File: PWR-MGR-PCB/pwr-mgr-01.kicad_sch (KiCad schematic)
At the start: 25 parts, among them J2 Battery_1x2, J3 USB_C_Receptacle_USB2.0_14P, U1 BQ24075, U5 USBLC6-2SC6, U6 TPS631011YBGR-Pin_Corrected

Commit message: Add MPNs and generate DRL file
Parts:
- C10: Manufacturer Part Number (none) -> CC0805MKX5R6BB476
- C3: Manufacturer Part Number (none) -> 08056D107MAT2A
- C4, C6: Manufacturer Part Number (none) -> CL21B475KBB6PNE
- C5: Manufacturer Part Number (none) -> KAF21KR71H105JU
- C9: Manufacturer Part Number (none) -> KAM21AT70J226MU
- D1, D2: Manufacturer Part Number (none) -> SML-D12U1WT86
- D3: Manufacturer Part Number (none) -> DIOM7959X265N
- J2: footprint Connector_JST:JST_PH_B2B-PH-K_1x02_P2.00mm_Vertical -> Connector_JST:JST_XH_B2B-XH-A_1x02_P2.50mm_Vertical; Manufacturer Part Number (none) -> B2B-XH-A
- J3: Manufacturer Part Number (none) -> USB4105-GF-A
- L2: Manufacturer Part Number (none) -> DFE18SAN1R0ME0L
- R1: Manufacturer Part Number (none) -> ERJ-U06D1181V
- R12, R13: Manufacturer Part Number (none) -> ERA-6ARB512V
- R17: Manufacturer Part Number (none) -> ERA-6ARB913V
- R18: Manufacturer Part Number (none) -> CR0805-FX-5113ELF
- R2: Manufacturer Part Number (none) -> PAT0805E1131BST1
- R3: Manufacturer Part Number (none) -> ERA-6AED4642V
- R4: Manufacturer Part Number (none) -> MCU0805MD1002BP500
- R5, R6: Manufacturer Part Number (none) -> RT73F2A1K5BTD
- U1: Manufacturer Part Number (none) -> BQ24075RGTR
- U5: Manufacturer Part Number (none) -> USBLC6-2SC6
- U6: Manufacturer Part Number (none) -> TPS631011YBGR
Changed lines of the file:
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@@
 			)
 		)
+		(property "Manufacturer Part Number" "RT73F2A1K5BTD"
+			(at 115.57 123.19 90)
+			(effects
+				(font
+					(size 1.27 1.27)
+				)
+				(hide yes)
+			)
+		)
 		(pin "2"
 		)
@@
 			)
 		)
+		(property "Manufacturer Part Number" "CC0805MKX5R6BB476"
+			(at 248.92 83.82 0)
+			(effects
+				(font
+					(size 1.27 1.27)
+				)
+				(hide yes)
+			)
+		)
 		(pin "2"
 		)
@@
 			)
 		)
+		(property "Manufacturer Part Number" "TPS631011YBGR"
+			(at 187.96 76.2 0)
+			(effects
+				(font
+					(size 1.27 1.27)
+				)
+				(hide yes)
+			)
+		)
 		(pin "A1"
 		)
@@
 			)
 		)
+		(property "Manufacturer Part Number" "DIOM7959X265N"
+			(at 83.82 66.04 0)
+			(effects
+				(font
+					(size 1.27 1.27)
+				)
+				(hide yes)
+			)
+		)
 		(pin "1"
 		)
@@
 			)
 		)
+		(property "Manufacturer Part Number" "KAM21AT70J226MU"
+			(at 170.18 86.36 0)
+			(effects
+				(font
+					(size 1.27 1.27)
+				)
+				(hide yes)
+			)
+		)
 		(pin "2"
 		)
@@
 			)
 		)
+		(property "Manufacturer Part Number" "USB4105-GF-A"
+			(at 53.34 81.28 0)
+			(effects
+				(font
+					(size 1.27 1.27)
+				)
+				(hide yes)
+			)
+		)
 		(pin "A12"
 		)
@@
 			)
 		)
+		(property "Manufacturer Part Number" "ERA-6ARB512V"
+			(at 78.74 73.66 90)
+			(effects
+				(font
+					(size 1.27 1.27)
+				)
+				(hide yes)
+			)
+		)
 		(pin "1"
 		)
@@
 			)
 		)
+		(property "Manufacturer Part Number" "ERA-6ARB913V"
+			(at 236.22 69.85 90)
+			(effects
+				(font
+					(size 1.27 1.27)
+				)
+				(hide yes)
+			)
+		)
 		(pin "2"
 		)
@@
 			)
 		)
+		(property "Manufacturer Part Number" "DFE18SAN1R0ME0L"
+			(at 208.28 102.87 0)
+			(effects
+				(font
+					(size 1.27 1.27)
+				)
+				(hide yes)
+			)
+		)
 		(pin "2"
 		)
@@
 			)
 		)
+		(property "Manufacturer Part Number" "ERA-6AED4642V "
+			(at 80.01 181.61 90)
+			(effects
+				(font
+					(size 1.27 1.27)
+				)
+				(hide yes)
+			)
+		)
 		(pin "2"
 		)
@@
 			)
 		)
+		(property "Manufacturer Part Number" "SML-D12U1WT86"
+			(at 105.41 123.19 0)
+			(effects
+				(font
+					(size 1.27 1.27)
+				)
+				(hide yes)
+			)
+		)
 		(pin "C"
 		)
@@
 			)
 		)
+		(property "Manufacturer Part Number" "BQ24075RGTR"
+			(at 85.09 157.48 0)
+			(effects
+				(font
+					(size 1.27 1.27)
+				)
+				(hide yes)
+			)
+		)
 		(pin "16"
 		)
@@
 			)
 		)
+		(property "Manufacturer Part Number" "MCU0805MD1002BP500 "
+			(at 60.96 160.02 90)
+			(effects
+				(font
+					(size 1.27 1.27)
+				)
+				(hide yes)
+			)
+		)
 		(pin "1"
 		)
@@
 			)
 		)
+		(property "Manufacturer Part Number" "RT73F2A1K5BTD"
+			(at 115.57 132.08 90)
+			(effects
+				(font
+					(size 1.27 1.27)
+				)
+				(hide yes)
+			)
+		)
 		(pin "2"
 		)
@@
 			)
 		)
+		(property "Manufacturer Part Number" "PAT0805E1131BST1"
+			(at 92.71 181.61 90)
+			(effects
+				(font
+					(size 1.27 1.27)
+				)
+				(hide yes)
+			)
+		)
 		(pin "1"
 		)
@@
 			)
 		)
+		(property "Manufacturer Part Number" "CR0805-FX-5113ELF"
+			(at 236.22 76.2 90)
+			(effects
+				(font
+					(size 1.27 1.27)
+				)
+				(hide yes)
+			)
+		)
 		(pin "2"
 		)
@@
 			)
 		)
+		(property "Manufacturer Part Number" "CL21B475KBB6PNE"
+			(at 114.3 144.78 0)
+			(effects
+				(font
+					(size 1.27 1.27)
+				)
+				(hide yes)
+			)
+		)
 		(pin "2"
 		)
@@
 			)
 		)
+		(property "Manufacturer Part Number" "USBLC6-2SC6"
+			(at 124.46 74.93 0)
+			(effects
+				(font
+					(size 1.27 1.27)
+				)
+				(hide yes)
+			)
+		)
 		(pin "3"
 		)
@@
 			)
 		)
+		(property "Manufacturer Part Number" "08056D107MAT2A"
+			(at 137.16 66.04 90)
+			(effects
+				(font
+					(size 1.27 1.27)
+				)
+				(hide yes)
+			)
+		)
 		(pin "2"
 		)
@@
 			)
 		)
+		(property "Manufacturer Part Number" "SML-D12U1WT86"
+			(at 104.14 132.08 0)
+			(effects
+				(font
+					(size 1.27 1.27)
+				)
+				(hide yes)
+			)
+		)
 		(pin "C"
 		)
@@
 			)
 		)
-		(property "Footprint" "Connector_JST:JST_PH_B2B-PH-K_1x02_P2.00mm_Vertical"
+		(property "Footprint" "Connector_JST:JST_XH_B2B-XH-A_1x02_P2.50mm_Vertical"
 			(at 46.99 165.1 0)
 			(effects
@@
 			)
 		)
+		(property "Manufacturer Part Number" " B2B-XH-A"
+			(at 46.99 165.1 0)
+			(effects
+				(font
+					(size 1.27 1.27)
+				)
+				(hide yes)
+			)
+		)
 		(pin "1"
 		)
@@
 			)
 		)
+		(property "Manufacturer Part Number" "KAF21KR71H105JU"
+			(at 60.96 146.05 0)
+			(effects
+				(font
+					(size 1.27 1.27)
+				)
+				(hide yes)
+			)
+		)
 		(pin "2"
 		)
@@
 			)
 		)
+		(property "Manufacturer Part Number" "ERJ-U06D1181V "
+			(at 85.09 181.61 90)
+			(effects
+				(font
+					(size 1.27 1.27)
+				)
+				(hide yes)
+			)
+		)
 		(pin "2"
 		)
@@
 			)
 		)
+		(property "Manufacturer Part Number" "CL21B475KBB6PNE"
+			(at 60.96 168.91 0)
+			(effects
+				(font
+					(size 1.27 1.27)
+				)
+				(hide yes)
+			)
+		)
 		(pin "2"
 		)
@@
 			(effects
 				(font
+					(size 1.27 1.27)
+				)
+				(hide yes)
+			)
+		)
+		(property "Manufacturer Part Number" "ERA-6ARB512V"
+			(at 87.63 71.12 90)
+			(effects
+				(font

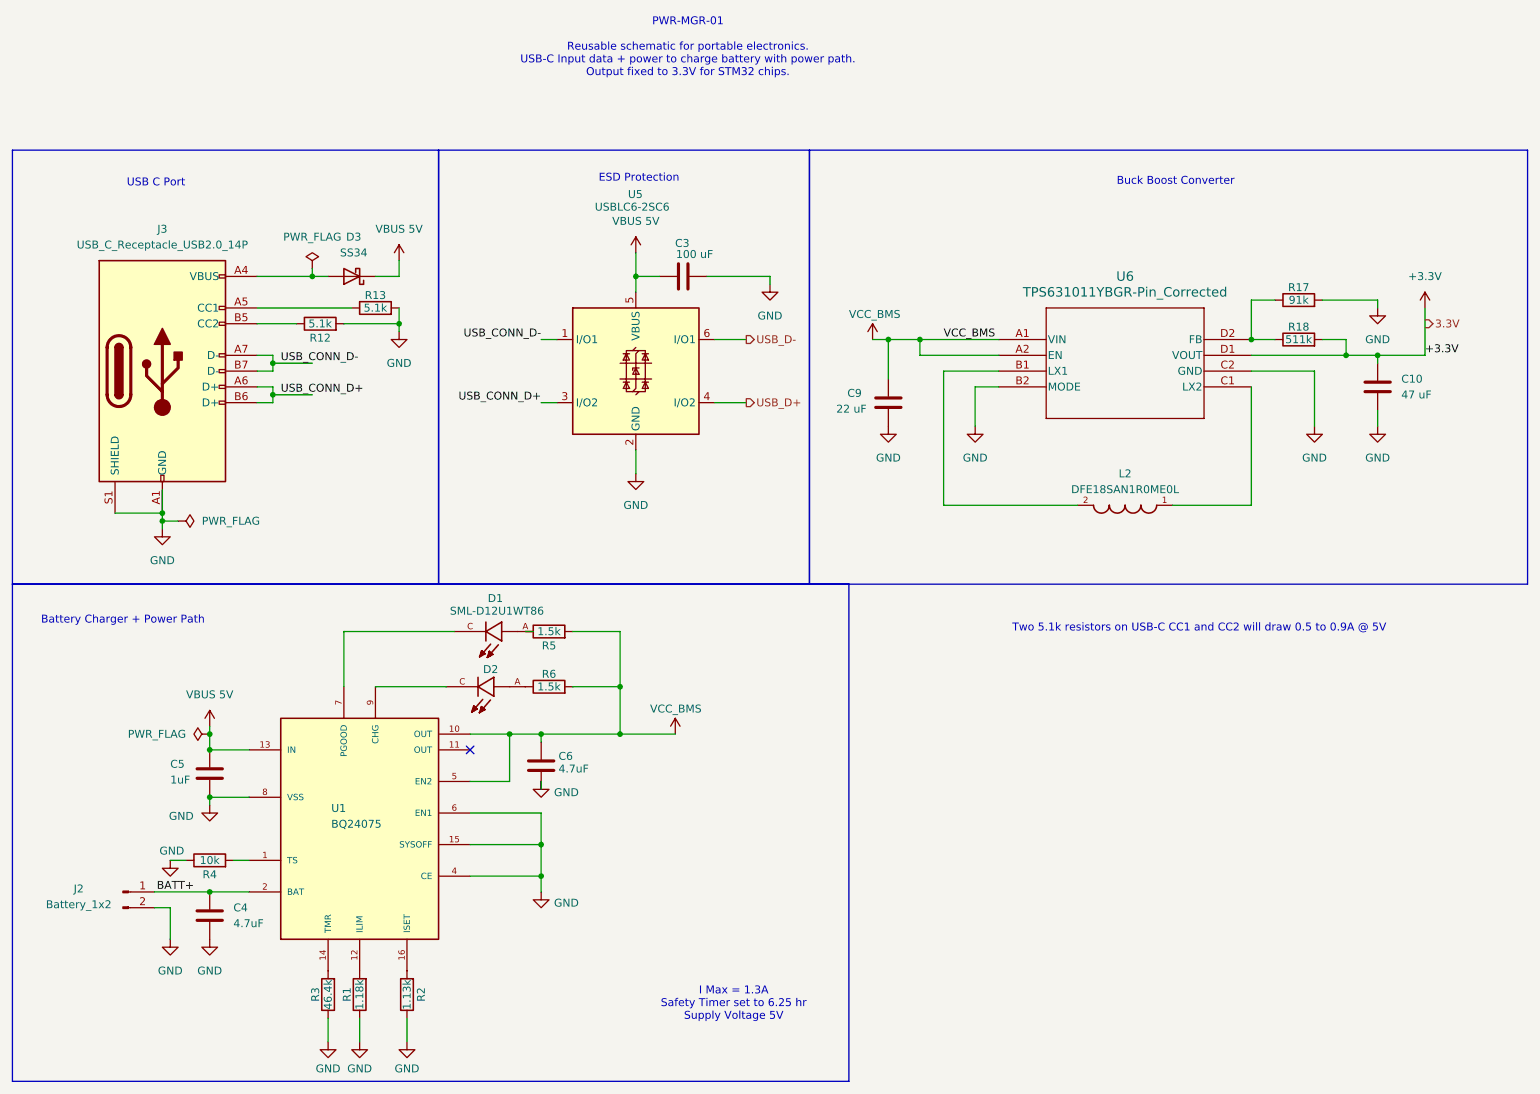
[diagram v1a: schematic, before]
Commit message: Adjust boost converter FB pin
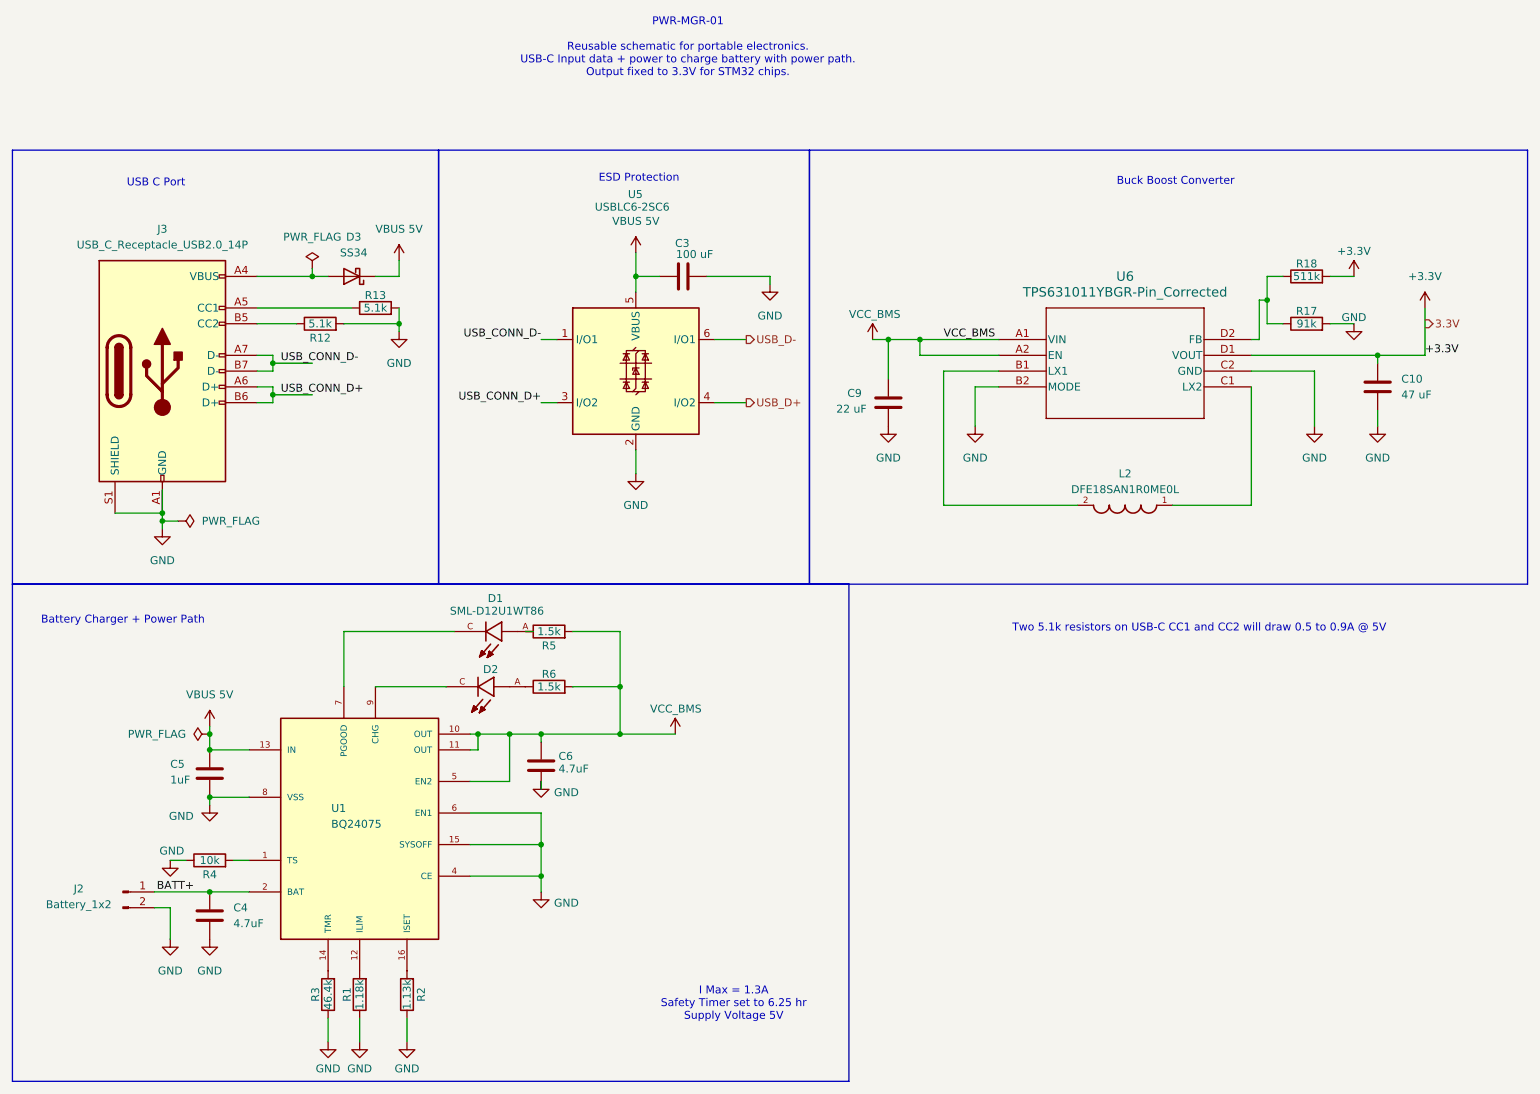
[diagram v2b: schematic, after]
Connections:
- net VCC_BMS: now also U1.11 (OUT)
- no-connect marks 1 -> 0
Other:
- moved on the sheet: R17, R18

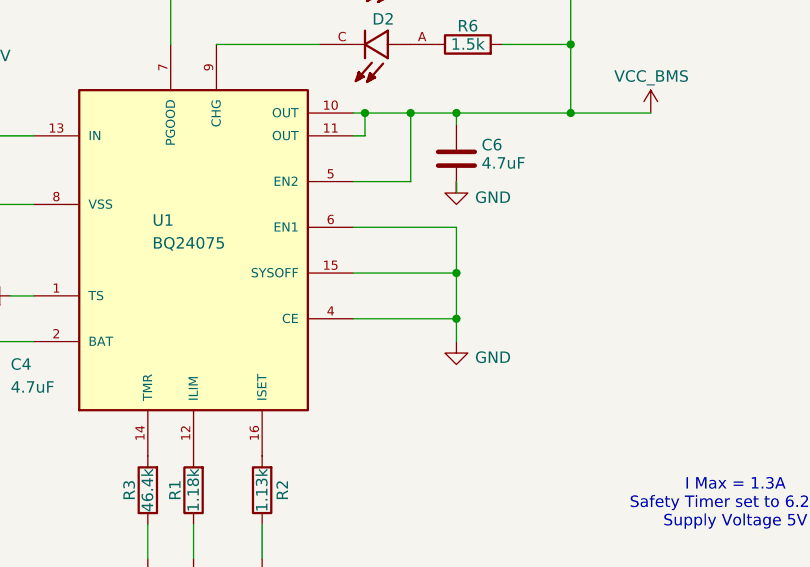
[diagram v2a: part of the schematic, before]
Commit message: Pull down SYSOFF
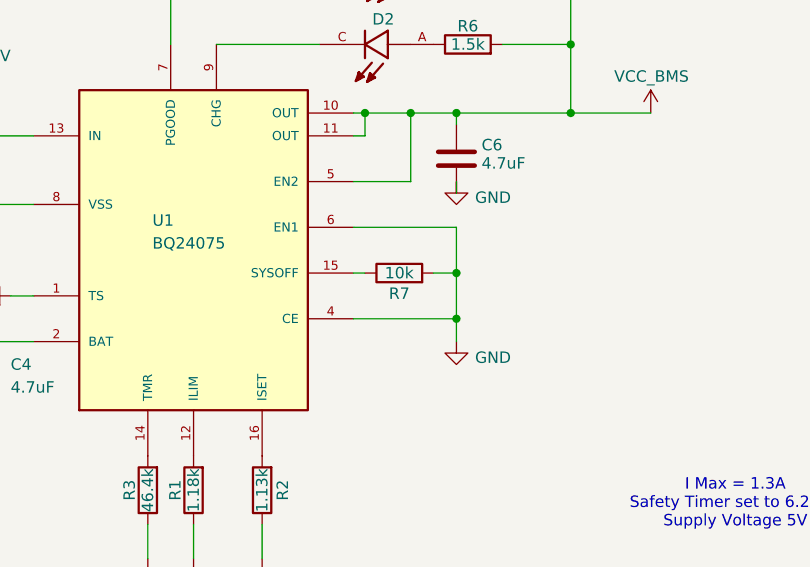
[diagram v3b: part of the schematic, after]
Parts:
- added R7: 10k, Resistor_SMD:R_0805_2012Metric, symbol Device:R
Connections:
- net GND: now also R7.2; no longer U1.15 (SYSOFF)
- new net: R7.1, U1.15 (SYSOFF)
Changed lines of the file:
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@@
 	(wire
 		(pts
+			(xy 111.76 157.48) (xy 114.3 157.48)
+		)
+		(stroke
+			(width 0)
+			(type default)
+		)
+	)
+	(wire
+		(pts
 			(xy 52.07 167.64) (xy 54.61 167.64)
 		)
@@
 	(wire
 		(pts
-			(xy 102.87 157.48) (xy 114.3 157.48)
+			(xy 102.87 157.48) (xy 104.14 157.48)
 		)
 		(stroke
@@
 					(unit 1)
 				)
+			)
+		)
+	)
+	(symbol
+		(lib_id "Device:R")
+		(at 107.95 157.48 90)
+		(unit 1)
+		(exclude_from_sim no)
+		(in_bom yes)
+		(on_board yes)
+		(dnp no)
+		(property "Reference" "R7"
+			(at 107.95 159.766 90)
+			(effects
+				(font
+					(size 1.27 1.27)
+				)
+			)
+		)
+		(property "Value" "10k"
+			(at 107.95 157.48 90)
+			(effects
+				(font
+					(size 1.27 1.27)
+				)
+			)
+		)
+		(property "Footprint" "Resistor_SMD:R_0805_2012Metric"
+			(at 107.95 159.258 90)
+			(effects
+				(font
+					(size 1.27 1.27)
+				)
+				(hide yes)
+			)
+		)
+		(property "Datasheet" "~"
+			(at 107.95 157.48 0)
+			(effects
+				(font
+					(size 1.27 1.27)
+				)
+				(hide yes)
+			)
+		)
+		(property "Description" "Resistor"
+			(at 107.95 157.48 0)
+			(effects
+				(font
+					(size 1.27 1.27)
+				)
+				(hide yes)
+			)
+		)
+		(property "Manufacturer Part Number" "MCU0805MD1002BP500 "
+			(at 107.95 157.48 90)
+			(effects
+				(font
+					(size 1.27 1.27)
+				)
+				(hide yes)
+			)
+		)
+		(pin "1"
+		)
+		(pin "2"
+		)
+		(instances
+			(project "PWR-MGR-PCB"
+				(path "/16b2e4e2-6399-42b6-a8e6-a11780888710/aa25d2a4-7317-40e7-833e-e05b81834ee4"
+					(reference "R7")
+					(unit 1)
+				)
